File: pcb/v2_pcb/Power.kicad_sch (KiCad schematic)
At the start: 41 parts, among them Q3 NMOS, Q4 NMOS, Q5 NMOS, U6 BQ25798RQMR, U7 MAX17320G22+

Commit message: fnish micro sd card
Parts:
- added BT1, BT2: Battery_Cell, symbol Device:Battery_Cell
- added C12, C8: 10nF, symbol Device:C_Small
- added C13, C14: 100nF, symbol Device:C_Small
- added C15, C16, C17: 470nF, symbol Device:C_Small
- added R11, R12: 68, symbol Device:R_Small_US
- added R13: 5m, symbol Device:R_Small_US
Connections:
- net GND: now also U7.14 (CSN), R13.2
- net GND1: now also U7.15 (CSP), U7.20 (GND), U7.25 (EPAD), BT2.2 (-), C12.2, C14.2, C15.2, C16.2, C17.2, R13.1
- net at R10.2, U7.1 (IN): now also C13.2, C14.1
- net at U7.12 (AOLDO): now also C17.1
- net at U7.13 (REG3): now also C15.1
- net at U7.17 (REG2): now also C16.1
- net at U7.2 (CP): now also C13.1
- net at U7.21 (CELL1): now also U7.22 (CELL2), U7.23 (CELL3), C12.1, C8.2, R12.2
- net at U7.24 (BATTS): now also C8.1, R11.2
- net at C7.1, Q4.3 (S), R10.1: now also BT1.1 (+), R11.1
- new net: BT1.2 (-), BT2.1 (+), R12.1
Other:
- moved on the sheet: R10

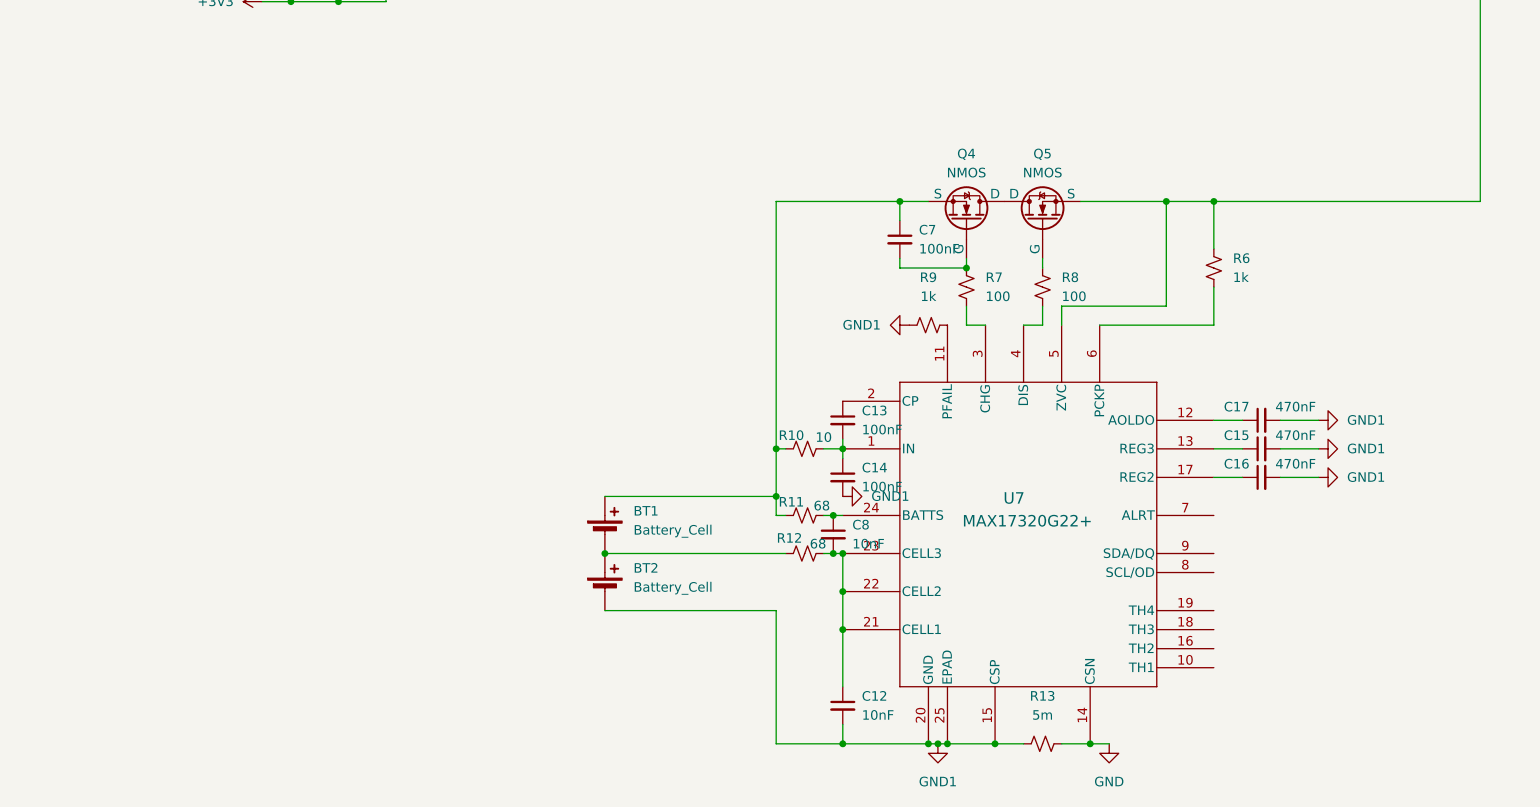
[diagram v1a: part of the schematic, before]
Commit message: done with max17320
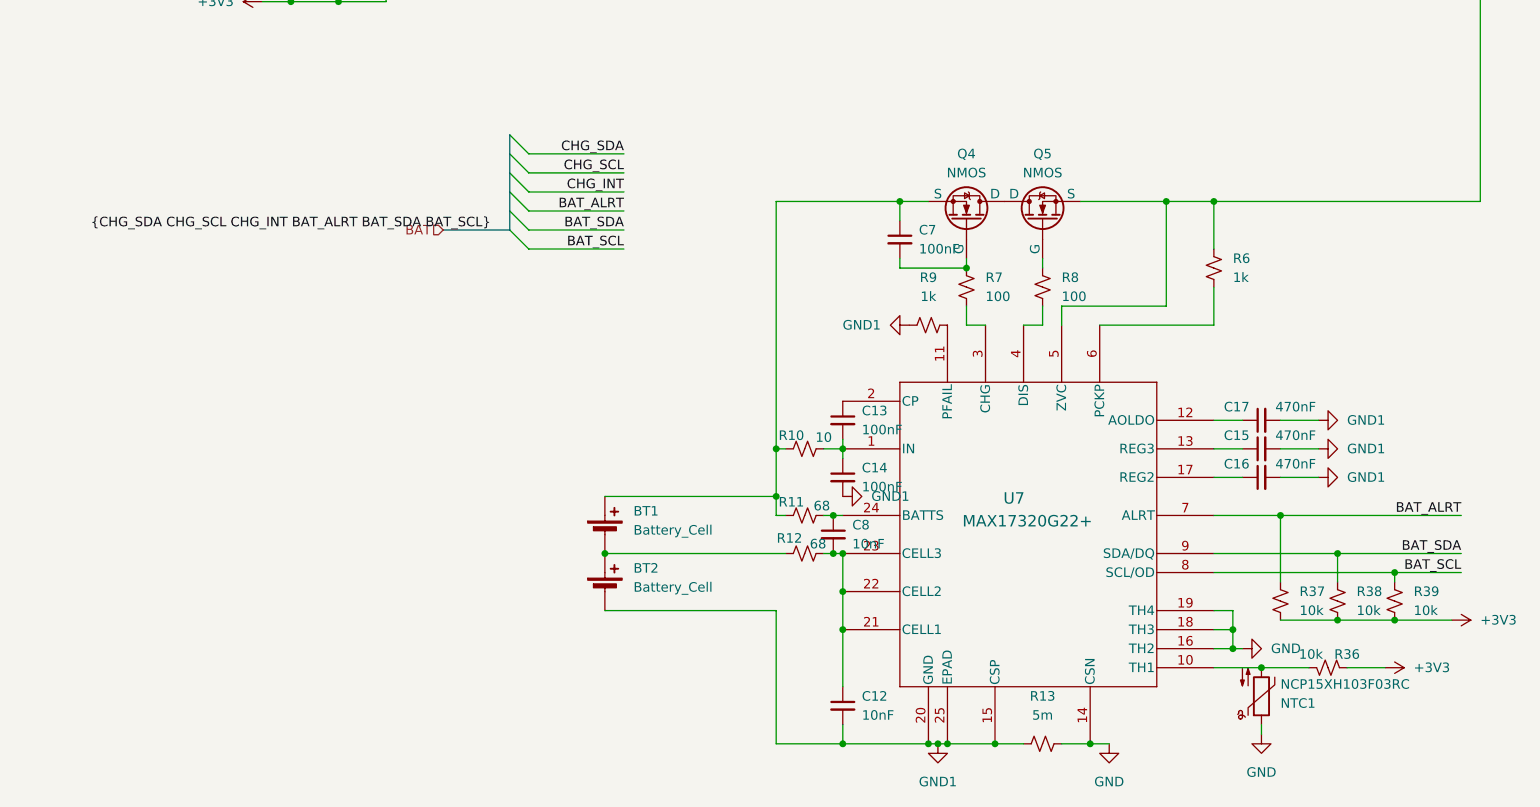
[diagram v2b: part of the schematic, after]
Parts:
- added NTC1: NCP15XH103F03RC, symbol Device:Thermistor_NTC
- added R36, R37, R38, R39: 10k, symbol Device:R_Small_US
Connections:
- net +3V3: now also R36.2, R37.2, R38.2, R39.2
- net GND: now also U7.16 (TH2), U7.18 (TH3), U7.19 (TH4), NTC1.1
- net at U7.10 (TH1): now also NTC1.2, R36.1
- net BAT_ALRT: now reaches U7.7 (ALRT)
- net BAT_ALRT: now also R37.1
- net BAT_SCL: now reaches U7.8 (SCL/OD)
- net BAT_SCL: now also R39.1
- net BAT_SDA: now reaches U7.9 (SDA/DQ)
- net BAT_SDA: now also R38.1

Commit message: working on
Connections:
- net GND: now also U6.10 (ACDRV2), U6.11 (ACDRV1); no longer U6.8 (VAC2), U6.9 (VAC1)
- net at C10.2, C11.2, C42.2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: now also U6.8 (VAC2), U6.9 (VAC1); no longer U6.10 (ACDRV2), U6.11 (ACDRV1)
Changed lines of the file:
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@@
+	)
+	(junction
+		(at 182.88 152.4)
+		(diameter 0)
+		(color 0 0 0 0)
+	)
+	(junction
+		(at 154.94 53.34)
+		(diameter 0)
+		(color 0 0 0 0)
+	)
+	(junction
+		(at 82.55 66.04)
+		(diameter 0)
+		(color 0 0 0 0)
+	)
+	(junction
+		(at 138.43 53.34)
+		(diameter 0)
+		(color 0 0 0 0)
+	)
+	(junction
+		(at 133.35 224.79)
+		(diameter 0)
+		(color 0 0 0 0)
+	)
+	(junction
+		(at 129.54 88.9)
+		(diameter 0)
+		(color 0 0 0 0)
+	)
+	(junction
+		(at 149.86 161.29)
+		(diameter 0)
+		(color 0 0 0 0)
+	)
+	(junction
+		(at 185.42 209.55)
+		(diameter 0)
+		(color 0 0 0 0)
+	)
+	(junction
+		(at 162.56 53.34)
+		(diameter 0)
+		(color 0 0 0 0)
+	)
+	(junction
+		(at 50.8 68.58)
+		(diameter 0)
+		(color 0 0 0 0)
+	)
+	(junction
+		(at 199.39 199.39)
+		(diameter 0)
+		(color 0 0 0 0)
+	)
+	(junction
+		(at 129.54 58.42)
+		(diameter 0)
+		(color 0 0 0 0)
+	)
+	(junction
+		(at 68.58 68.58)
+		(diameter 0)
+		(color 0 0 0 0)
+	)
+	(junction
+		(at 50.8 63.5)
+		(diameter 0)
+		(color 0 0 0 0)
+	)
+	(junction
+		(at 124.46 191.77)
+		(diameter 0)
+		(color 0 0 0 0)
+	)
+	(junction
+		(at 199.39 208.28)
+		(diameter 0)
+		(color 0 0 0 0)
+	)
+	(junction
+		(at 73.66 92.71)
+		(diameter 0)
+		(color 0 0 0 0)
+	)
+	(junction
+		(at 66.04 125.73)
+		(diameter 0)
+		(color 0 0 0 0)
+	)
+	(junction
+		(at 135.89 110.49)
+		(diameter 0)
+		(color 0 0 0 0)
+	)
+	(junction
+		(at 148.59 83.82)
+		(diameter 0)
+		(color 0 0 0 0)
+	)
+	(junction
+		(at 185.42 212.09)
+		(diameter 0)
+		(color 0 0 0 0)
+	)
+	(junction
+		(at 148.59 88.9)
+		(diameter 0)
+		(color 0 0 0 0)
+	)
+	(junction
+		(at 130.81 96.52)
+		(diameter 0)
+		(color 0 0 0 0)
+	)
+	(junction
+		(at 139.7 88.9)
+		(diameter 0)
+		(color 0 0 0 0)
+	)
+	(junction
+		(at 133.35 185.42)
+		(diameter 0)
+		(color 0 0 0 0)
+	)
+	(junction
+		(at 72.39 116.84)
+		(diameter 0)
+		(color 0 0 0 0)
+	)
+	(junction
+		(at 147.32 53.34)
+		(diameter 0)
+		(color 0 0 0 0)
+	)
+	(junction
+		(at 73.66 100.33)
+		(diameter 0)
+		(color 0 0 0 0)
+	)
+	(junction
+		(at 160.02 104.14)
+		(diameter 0)
+		(color 0 0 0 0)
 	)
 	(junction
 		(at 162.56 71.12)
-		(diameter 0)
-		(color 0 0 0 0)
-	)
-	(junction
-		(at 154.94 53.34)
-		(diameter 0)
-		(color 0 0 0 0)
-	)
-	(junction
-		(at 82.55 66.04)
-		(diameter 0)
-		(color 0 0 0 0)
-	)
-	(junction
-		(at 182.88 152.4)
-		(diameter 0)
-		(color 0 0 0 0)
-	)
-	(junction
-		(at 138.43 53.34)
-		(diameter 0)
-		(color 0 0 0 0)
-	)
-	(junction
-		(at 133.35 224.79)
-		(diameter 0)
-		(color 0 0 0 0)
-	)
-	(junction
-		(at 129.54 88.9)
-		(diameter 0)
-		(color 0 0 0 0)
-	)
-	(junction
-		(at 149.86 161.29)
-		(diameter 0)
-		(color 0 0 0 0)
-	)
-	(junction
-		(at 185.42 209.55)
-		(diameter 0)
-		(color 0 0 0 0)
-	)
-	(junction
-		(at 162.56 53.34)
-		(diameter 0)
-		(color 0 0 0 0)
-	)
-	(junction
-		(at 50.8 68.58)
-		(diameter 0)
-		(color 0 0 0 0)
-	)
-	(junction
-		(at 199.39 199.39)
-		(diameter 0)
-		(color 0 0 0 0)
-	)
-	(junction
-		(at 129.54 58.42)
-		(diameter 0)
-		(color 0 0 0 0)
-	)
-	(junction
-		(at 68.58 68.58)
-		(diameter 0)
-		(color 0 0 0 0)
-	)
-	(junction
-		(at 50.8 63.5)
-		(diameter 0)
-		(color 0 0 0 0)
-	)
-	(junction
-		(at 124.46 191.77)
-		(diameter 0)
-		(color 0 0 0 0)
-	)
-	(junction
-		(at 199.39 208.28)
-		(diameter 0)
-		(color 0 0 0 0)
-	)
-	(junction
-		(at 73.66 92.71)
-		(diameter 0)
-		(color 0 0 0 0)
-	)
-	(junction
-		(at 66.04 125.73)
-		(diameter 0)
-		(color 0 0 0 0)
-	)
-	(junction
-		(at 135.89 110.49)
-		(diameter 0)
-		(color 0 0 0 0)
-	)
-	(junction
-		(at 148.59 83.82)
-		(diameter 0)
-		(color 0 0 0 0)
-	)
-	(junction
-		(at 185.42 212.09)
-		(diameter 0)
-		(color 0 0 0 0)
-	)
-	(junction
-		(at 148.59 88.9)
-		(diameter 0)
-		(color 0 0 0 0)
-	)
-	(junction
-		(at 130.81 96.52)
-		(diameter 0)
-		(color 0 0 0 0)
-	)
-	(junction
-		(at 139.7 88.9)
-		(diameter 0)
-		(color 0 0 0 0)
-	)
-	(junction
-		(at 133.35 185.42)
-		(diameter 0)
-		(color 0 0 0 0)
-	)
-	(junction
-		(at 72.39 116.84)
-		(diameter 0)
-		(color 0 0 0 0)
-	)
-	(junction
-		(at 147.32 53.34)
-		(diameter 0)
-		(color 0 0 0 0)
-	)
-	(junction
-		(at 73.66 100.33)
-		(diameter 0)
-		(color 0 0 0 0)
-	)
-	(junction
-		(at 160.02 104.14)
 		(diameter 0)
 		(color 0 0 0 0)
@@
 	(wire
 		(pts
-			(xy 162.56 58.42) (xy 177.8 58.42)
+			(xy 162.56 58.42) (xy 240.03 58.42)
 		)
 		(stroke
@@
 	(wire
 		(pts
+			(xy 162.56 71.12) (xy 182.88 71.12)
+		)
+		(stroke
+			(width 0)
+			(type default)
+		)
+	)
+	(wire
+		(pts
 			(xy 160.02 168.91) (xy 160.02 166.37)
 		)
@@
 	(wire
 		(pts
-			(xy 182.88 152.4) (xy 218.44 152.4)
-		)
-		(stroke
-			(width 0)
-			(type default)
-		)
-	)
-	(wire
-		(pts
 			(xy 191.77 194.31) (xy 215.9 194.31)
 		)
@@
 	(wire
 		(pts
-			(xy 162.56 71.12) (xy 218.44 71.12)
-		)
-		(stroke
-			(width 0)
-			(type default)
-		)
-	)
-	(wire
-		(pts
 			(xy 132.08 199.39) (xy 133.35 199.39)
 		)
@@
 	(wire
 		(pts
-			(xy 218.44 71.12) (xy 218.44 152.4)
+			(xy 182.88 71.12) (xy 182.88 152.4)
 		)
 		(stroke
@@
 	)
 	(label "vpack+"
-		(at 180.34 71.12 180)
+		(at 172.72 71.12 180)
 		(effects
 			(font

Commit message: add rpls for 1v8, 5v
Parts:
- removed R36: 10k, symbol Device:R_Small_US
- added C180, C183: 10uF 25V X7R, Capacitor_SMD:C_1206_3216Metric, symbol Device:C_Small
- added C181, C184: 22uF 10V X7R, Capacitor_SMD:C_1206_3216Metric, symbol Device:C_Small
- added C182: 22pF C0G, Capacitor_SMD:C_0603_1608Metric, symbol Device:C_Small
- added C185: 39pF C0G, Capacitor_SMD:C_0603_1608Metric, symbol Device:C_Small
- added C93: 10uF, symbol Device:C_Small
- added R221: 10k, Resistor_SMD:R_0603_1608Metric, symbol Device:R_Small_US
- added R222, R225: 1k, Resistor_SMD:R_0603_1608Metric, symbol Device:R_Small_US
- added R223, R226: 47k 1%, Resistor_SMD:R_0603_1608Metric, symbol Device:R_Small_US
- added R224: 37.4k 1%, Resistor_SMD:R_0603_1608Metric, symbol Device:R_Small_US
- added R227: 8.87k 1%, Resistor_SMD:R_0603_1608Metric, symbol Device:R_Small_US
- added U8, U9: RPL-3.0-R, symbol open-race:RPL-3.0-R
- L1: value L -> 2.2uH
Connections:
- net +3V3 is gone; now on net +3V3_MAIN: D2.2 (A), R29.2, R30.2, R31.2, R37.2, R38.2, R39.2
- net GND: now also C180.2, C181.2, C183.2, C184.2, C93.1, R224.2, R227.2, U8.3 (PGND), U8.4 (PGND), U8.8 (AGND), U9.3 (PGND), U9.4 (PGND), U9.8 (AGND); no longer NTC1.1, R24.2, U6.17 (ILIM_HIZ), U7.16 (TH2), U7.18 (TH3), U7.19 (TH4)
- net GND1: now also NTC1.1, U7.16 (TH2), U7.18 (TH3), U7.19 (TH4)
- net VSYS_RAW: now reaches C56.2, C62.2, C81.2, C82.2, C83.2, U6.25 (SYS)
- net VSYS_RAW: now also C180.1, C183.1, C93.2, U8.2 (VIN), U9.1 (CTRL), U9.2 (VIN)
- net +3V3_MAIN: now reaches NTC1.2, U7.10 (TH1)
- net +3V3_MAIN: now also R221.1
- new net: R24.2, U6.17 (ILIM_HIZ)
- new net: R222.1, U8.6 (+Sense)
- new net: C182.2, R223.2, R224.1, U8.7 (FB)
- new net: R225.1, U9.6 (+Sense)
- new net: C185.2, R226.2, R227.1, U9.7 (FB)
- new net +1V8_AON: C181.1, C182.1, R222.2, R223.1, U8.5 (VOUT)
- new net +5V_AUX: C184.1, C185.1, R225.2, R226.1, U9.5 (VOUT)
- new net BUCK_3V3_PG: R221.2, U8.1 (CTRL)
- no-connect marks 2 -> 6
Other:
- note added: "1.8 V AON BUCK — RPL-3.0-R"
- note added: "5 V AUX BUCK — RPL-3.0-R"
- note added: "POWER TREE — RPL BUCKS ADDED VSYS_RAW -> U8 (1.8 V) -> +1V8_AON; CTRL = BUCK_3V3_PG with +3V3_MAIN pull-up. VSYS_RAW -> U9 (5 V) -> +5V_AUX; CTRL tied to VIN. WARNING: the 5 V buck needs about 6.8 V input to regulate; validate the loaded 2S minimum. TPSM863253 3.3 V stage and +1V8_RUN load switch remain to be inserted."

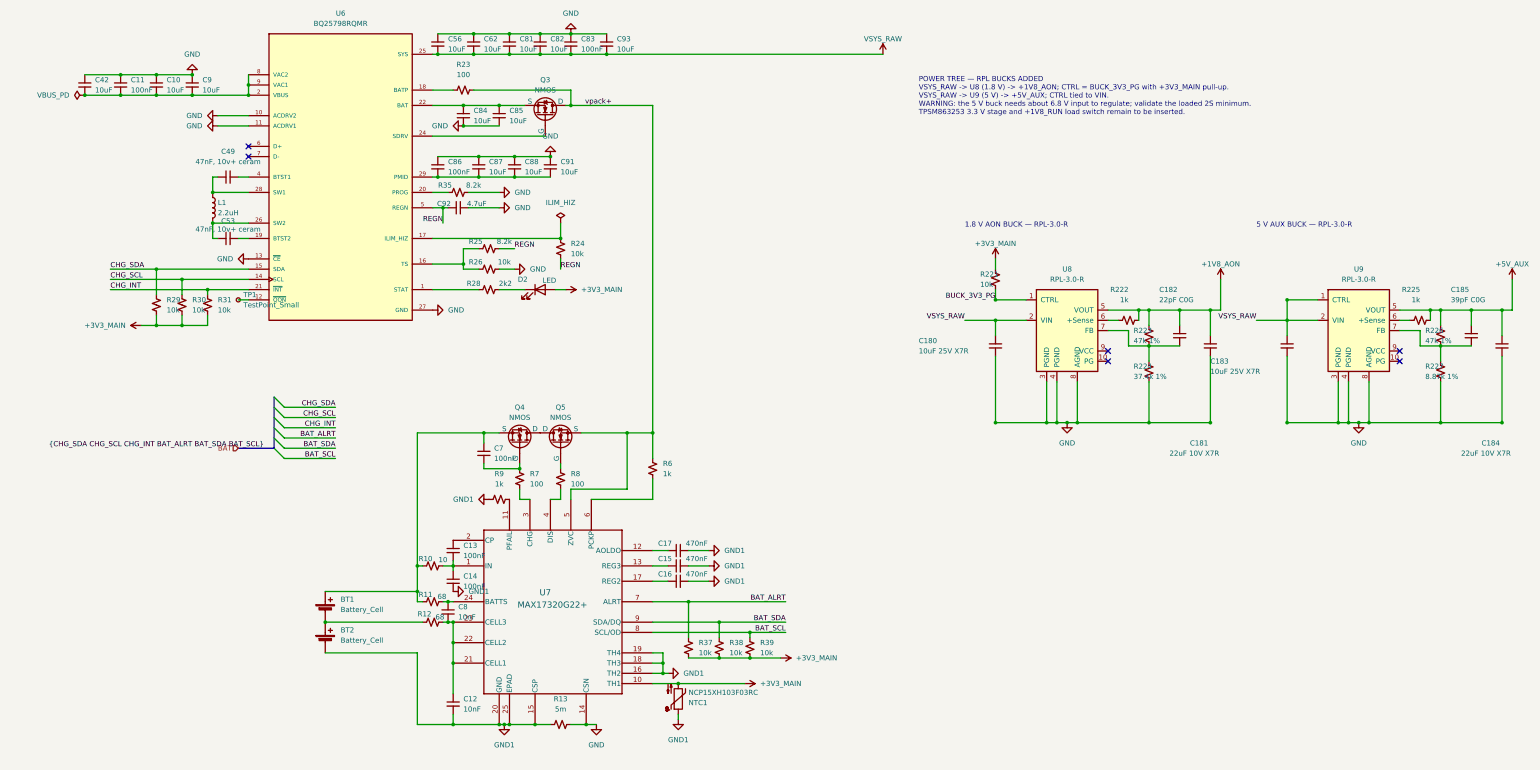
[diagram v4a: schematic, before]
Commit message: add tpsm buck stage
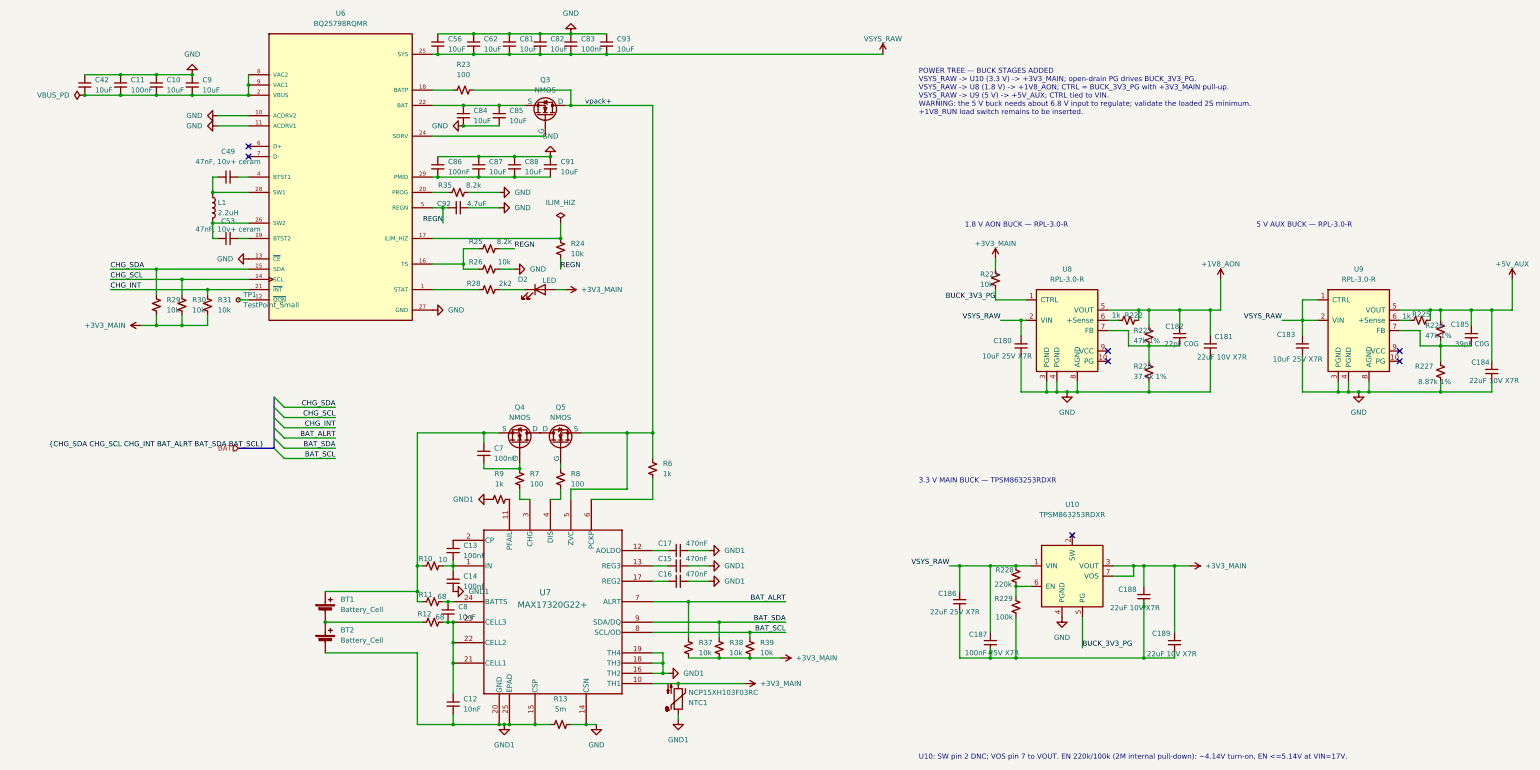
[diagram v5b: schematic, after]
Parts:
- added C186: 22uF 25V X7R, Capacitor_SMD:C_1206_3216Metric, symbol Device:C_Small
- added C187: 100nF 25V X7R, Capacitor_SMD:C_0603_1608Metric, symbol Device:C_Small
- added C188, C189: 22uF 10V X7R, Capacitor_SMD:C_1206_3216Metric, symbol Device:C_Small
- added R228: 220k, Resistor_SMD:R_0603_1608Metric, symbol Device:R_Small_US
- added R229: 100k, Resistor_SMD:R_0603_1608Metric, symbol Device:R_Small_US
- added U10: TPSM863253RDXR, Package_DFN_QFN:Texas_RDX0007A_QFN-FCMOD-7-3.3x4mm-P0.5mm_4EP, symbol open-race:TPSM863253RDXR
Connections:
- net +3V3_MAIN: now also C188.1, C189.1, U10.3 (VOUT), U10.7 (VOS)
- net BUCK_3V3_PG: now also U10.5 (PG)
- net GND: now also U10.4 (PGND)
- net VSYS_RAW: now also C186.1, C187.1, R228.1, U10.1 (VIN)
- new net: R228.2, R229.1, U10.6 (EN)
- new net: C186.2, C187.2, C188.2, C189.2, R229.2
- no-connect marks 6 -> 7
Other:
- note added: "3.3 V MAIN BUCK — TPSM863253RDXR"
- note added: "POWER TREE — BUCK STAGES ADDED VSYS_RAW -> U10 (3.3 V) -> +3V3_MAIN; open-drain PG drives BUCK_3V3_PG. VSYS_RAW -> U8 (1.8 V) -> +1V8_AON; CTRL = BUCK_3V3_PG with +3V3_MAIN pull-up. VSYS_RAW -> U9 (5 V) -> +5V_AUX; CTRL tied to VIN. WARNING: the 5 V buck needs about 6.8 V input to regulate; validate the loaded 2S minimum. +1V8_RUN load switch remains to be inserted."
- note added: "U10: SW pin 2 DNC; VOS pin 7 to VOUT. EN 220k/100k (2M internal pull-down): ~4.14V turn-on, EN <=5.14V at VIN=17V."
- note removed: "POWER TREE — RPL BUCKS ADDED VSYS_RAW -> U8 (1.8 V) -> +1V8_AON; CTRL = BUCK_3V3_PG with +3V3_MAIN pull-up. VSYS_RAW -> U9 (5 V) -> +5V_AUX; CTRL tied to VIN. WARNING: the 5 V buck needs about 6.8 V input to regulate; validate the loaded 2S minimum. TPSM863253 3.3 V stage and +1V8_RUN load switch remain to be inserted."
- moved on the sheet: C180, C183, C184, R226
